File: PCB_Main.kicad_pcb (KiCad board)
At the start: 2 copper layers, 101.6 x 53.3 mm, 37 parts, among them J1 Power, J2 PWM, J3 Analog, J4 PWM, J5 Analog, J6 Communication, J7 Conn_01x03, J8 Conn_01x03, U1 DPS310, U2 ATP3012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

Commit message: update silk
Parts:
- 1PPS1: value LED -> 1PPS
- AE-MICRO-SD-DIP1: value Micro_SD_Card_Det_Hirose_DM3AT -> AE-MICRO-SD-DIP
- Air-UART1: value Conn_01x04_Female -> Air-UART
- Air1: value LED -> Air
- GPS-UART1: value Conn_01x05_Female -> GPS-UART
- ICS-UART1: value Conn_01x05_Female -> ICS-UART
- ICS1: value LED -> ICS
- M78AR05-1: renamed from U3; value R-78E5.0-1.0 -> M78AR05
- M78AR05-2: renamed from U5; value R-78E5.0-1.0 -> M78AR05
- M78AR05-3: renamed from U4; value R-78E5.0-1.0 -> M78AR05
- Power1: value LED -> Power
- SD1: value LED -> SD
- Speaker1: value Conn_01x03_Female -> Speaker
- Under-UART1: value Conn_01x04_Female -> Under-UART
- Under1: value LED -> Under
- renumbered U6 to AE-BNO55, U2 to ATP3012, U1 to DPS310, U7 to ICS-board1
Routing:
- net L_Air: track 43.7 -> 45.1 mm
- net L_ICS: track 21.0 -> 21.9 mm
- added copper zone on B.Cu, net GND
- added copper zone on F.Cu, net GND

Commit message: pass DRC
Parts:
- moved Power1 3.18 mm to (124.8, 97.5), turned to 180 degrees
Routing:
- net 3.3V: track 182.2 -> 184.5 mm
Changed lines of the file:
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@@
     (pad_to_mask_clearance 0)
     (aux_axis_origin 100 100)
-    (grid_origin 100 100)
     (pcbplotparams
       (layerselection 0x0000030_80000001)
@@
   )
   (footprint "LED_THT:LED_D3.0mm_Clear" (layer "F.Cu")
-    (at 121.59 97.46)
+    (at 124.77 97.46 180)
     (descr "IR-LED, diameter 3.0mm, 2 pins, color: clear")
     (tags "IR infrared LED diameter 3.0mm 2 pins clear")
@@
       (effects (font (size 1 1) (thickness 0.15)))
     )
-    (fp_text value "Power" (at -3.175 0) (layer "F.SilkS")
+    (fp_text value "Power" (at 6.355 0) (layer "F.SilkS")
       (effects (font (size 1 1) (thickness 0.15)))
     )
@@
     (fp_arc (start -0.23 -1.16619) (mid 3.17 0.000452) (end -0.230555 1.165476) (layer "F.Fab") (width 0.1))
     (fp_circle (center 1.27 0) (end 2.77 0) (layer "F.Fab") (width 0.1) (fill none))
-    (pad "1" thru_hole rect (at 0 0) (size 1.8 1.8) (drill 0.9) (layers *.Cu *.Mask)
+    (pad "1" thru_hole rect (at 0 0 180) (size 1.8 1.8) (drill 0.9) (layers *.Cu *.Mask)
       (net 1 "GND") (pinfunction "K") (pintype "passive"))
-    (pad "2" thru_hole circle (at 2.54 0) (size 1.8 1.8) (drill 0.9) (layers *.Cu *.Mask)
+    (pad "2" thru_hole circle (at 2.54 0 180) (size 1.8 1.8) (drill 0.9) (layers *.Cu *.Mask)
       (net 47 "3.3V") (pinfunction "A") (pintype "passive"))
     (model "${KICAD6_3DMODEL_DIR}/LED_THT.3dshapes/LED_D3.0mm_Clear.wrl"
@@
   (segment (start 189.18 75.87) (end 189.26 75.79) (width 0.25) (layer "F.Cu") (net 1))
   (segment (start 145.64 87.3) (end 145.72 87.3) (width 0.25) (layer "F.Cu") (net 1))
-  (segment (start 119.68 93.655) (end 119.685 93.65) (width 0.25) (layer "F.Cu") (net 1))
   (segment (start 126.416 49.2) (end 128.321 51.105) (width 0.25) (layer "F.Cu") (net 1))
   (segment (start 178.555 83.04) (end 168.58 83.04) (width 0.25) (layer "F.Cu") (net 1))
@@
   (segment (start 141.275 51.105) (end 141.91 51.105) (width 0.25) (layer "F.Cu") (net 1))
   (segment (start 113.97 74.6) (end 116.51 74.6) (width 0.25) (layer "F.Cu") (net 1))
+  (segment (start 121.59 93.65) (end 107.62 93.65) (width 0.25) (layer "F.Cu") (net 1))
   (segment (start 189.26 59.32) (end 191.4 59.32) (width 0.25) (layer "F.Cu") (net 1))
   (segment (start 107.62 84.76) (end 107.62 92.38) (width 0.25) (layer "F.Cu") (net 1))
   (segment (start 107.62 92.38) (end 107.62 97.46) (width 0.25) (layer "F.Cu") (net 1))
   (segment (start 166.04 80.5) (end 168.58 83.04) (width 0.25) (layer "F.Cu") (net 1))
-  (segment (start 107.62 93.65) (end 119.685 93.65) (width 0.25) (layer "F.Cu") (net 1))
+  (segment (start 121.59 93.65) (end 124.765 93.65) (width 0.25) (layer "F.Cu") (net 1))
   (segment (start 157.15 56.82) (end 157.15 52.375) (width 0.25) (layer "F.Cu") (net 1))
   (segment (start 191.44 75.87) (end 189.34 75.87) (width 0.25) (layer "F.Cu") (net 1))
@@
   (segment (start 110.16 54.28) (end 108.89 54.28) (width 0.25) (layer "F.Cu") (net 1))
   (segment (start 141.91 51.105) (end 141.91 59.34) (width 0.25) (layer "F.Cu") (net 1))
-  (segment (start 119.685 93.65) (end 121.59 93.65) (width 0.25) (layer "F.Cu") (net 1))
   (segment (start 107.62 55.55) (end 107.615 55.545) (width 0.25) (layer "F.Cu") (net 1))
   (segment (start 141.275 51.105) (end 148.915 51.105) (width 0.25) (layer "F.Cu") (net 1))
@@
   (segment (start 153.35 60.62) (end 157.15 56.82) (width 0.25) (layer "F.Cu") (net 1))
   (segment (start 166.04 74.6) (end 166.04 80.5) (width 0.25) (layer "F.Cu") (net 1))
+  (segment (start 124.77 97.46) (end 124.77 93.655) (width 0.25) (layer "F.Cu") (net 1))
   (segment (start 134.45 93.65) (end 135.6 92.5) (width 0.25) (layer "F.Cu") (net 1))
   (segment (start 135.6 77.26) (end 135.6 72.1) (width 0.25) (layer "F.Cu") (net 1))
+  (segment (start 124.765 93.65) (end 134.45 93.65) (width 0.25) (layer "F.Cu") (net 1))
   (segment (start 107.62 92.38) (end 107.62 93.65) (width 0.25) (layer "F.Cu") (net 1))
   (segment (start 113.97 58.09) (end 116.51 58.09) (width 0.25) (layer "F.Cu") (net 1))
@@
   (segment (start 157.15 52.375) (end 155.88 51.105) (width 0.25) (layer "F.Cu") (net 1))
   (segment (start 145.72 94.92) (end 143.18 97.46) (width 0.25) (layer "F.Cu") (net 1))
-  (segment (start 121.59 93.65) (end 134.45 93.65) (width 0.25) (layer "F.Cu") (net 1))
   (segment (start 128.321 51.105) (end 141.275 51.105) (width 0.25) (layer "F.Cu") (net 1))
   (segment (start 189.34 75.87) (end 189.26 75.79) (width 0.25) (layer "F.Cu") (net 1))
@@
   (segment (start 113.97 88.57) (end 110.16 84.76) (width 0.25) (layer "F.Cu") (net 1))
   (segment (start 107.62 84.76) (end 110.16 84.76) (width 0.25) (layer "F.Cu") (net 1))
-  (segment (start 121.59 97.46) (end 121.59 93.65) (width 0.25) (layer "F.Cu") (net 1))
   (segment (start 191.4 59.32) (end 191.44 59.36) (width 0.25) (layer "F.Cu") (net 1))
   (segment (start 110.16 70.79) (end 113.97 74.6) (width 0.25) (layer "F.Cu") (net 1))
@@
   (segment (start 155.88 51.105) (end 148.915 51.105) (width 0.25) (layer "F.Cu") (net 1))
   (segment (start 153.34 68.25) (end 154.61 66.98) (width 0.25) (layer "F.Cu") (net 1))
+  (segment (start 124.77 93.655) (end 124.765 93.65) (width 0.25) (layer "F.Cu") (net 1))
   (segment (start 141.275 62.535) (end 136.195 62.535) (width 0.25) (layer "B.Cu") (net 1))
   (segment (start 189.26 75.79) (end 180.09 75.79) (width 0.25) (layer "B.Cu") (net 1))
@@
   (segment (start 144.45 84.125) (end 119.685 84.125) (width 0.25) (layer "B.Cu") (net 31))
   (segment (start 167.945 49.2) (end 164.77 52.375) (width 0.25) (layer "B.Cu") (net 31))
-  (segment (start 119.05 86.03) (end 116.51 86.03) (width 0.25) (layer "F.Cu") (net 32))
-  (segment (start 136.83 86.03) (end 119.05 86.03) (width 0.25) (layer "F.Cu") (net 32))
-  (segment (start 143.22 92.5) (end 136.83 86.11) (width 0.25) (layer "F.Cu") (net 32))
-  (segment (start 119.05 58.09) (end 119.05 86.03) (width 0.25) (layer "F.Cu") (net 32))
+  (segment (start 119.05 86.03) (end 116.51 86.03) (width 1) (layer "F.Cu") (net 32))
+  (segment (start 136.83 86.03) (end 119.05 86.03) (width 1) (layer "F.Cu") (net 32))
+  (segment (start 143.22 92.5) (end 136.83 86.11) (width 1) (layer "F.Cu") (net 32))
+  (segment (start 119.05 58.09) (end 119.05 86.03) (width 1) (layer "F.Cu") (net 32))
   (segment (start 136.83 86.11) (end 136.83 86.03) (width 0.25) (layer "F.Cu") (net 32))
-  (segment (start 116.51 55.55) (end 119.05 58.09) (width 0.25) (layer "F.Cu") (net 32))
-  (segment (start 116.51 72.06) (end 119.05 72.06) (width 0.25) (layer "F.Cu") (net 32))
+  (segment (start 116.51 55.55) (end 119.05 58.09) (width 1) (layer "F.Cu") (net 32))
+  (segment (start 116.51 72.06) (end 119.05 72.06) (width 1) (layer "F.Cu") (net 32))
   (segment (start 145.64 94.92) (end 145.72 94.92) (width 0.25) (layer "B.Cu") (net 32))
-  (segment (start 143.22 92.5) (end 145.64 94.92) (width 0.25) (layer "B.Cu") (net 32))
-  (segment (start 145.72 94.92) (end 145.72 97.46) (width 0.25) (layer "B.Cu") (net 32))
+  (segment (start 143.22 92.5) (end 145.64 94.92) (width 1) (layer "B.Cu") (net 32))
+  (segment (start 145.72 94.92) (end 145.72 97.46) (width 1) (layer "B.Cu") (net 32))
   (segment (start 110.16 87.3) (end 113.97 91.11) (width 0.25) (layer "F.Cu") (net 35))
   (segment (start 113.97 91.11) (end 116.51 91.11) (width 0.25) (layer "F.Cu") (net 35))
@@
   (segment (start 140.025 54.915) (end 145.73 60.62) (width 0.25) (layer "B.Cu") (net 47))
   (segment (start 178.105 88.57) (end 185.09 81.585) (width 0.25) (layer "B.Cu") (net 47))
-  (segment (start 124.13 97.46) (end 126.035 95.555) (width 0.25) (layer "B.Cu") (net 47))
   (segment (start 135.56 95.555) (end 136.83 94.285) (width 0.25) (layer "B.Cu") (net 47))
   (segment (start 145.73 60.62) (end 141.91 64.44) (width 0.25) (layer "B.Cu") (net 47))
@@
   (segment (start 140.68 92.5) (end 140.68 91.15) (width 0.25) (layer "B.Cu") (net 47))
   (segment (start 140.68 91.15) (end 140.64 91.11) (width 0.25) (layer "B.Cu") (net 47))
+  (segment (start 135.56 95.555) (end 123.495 95.555) (width 0.25) (layer "B.Cu") (net 47))
   (segment (start 160.97 58.08) (end 160.97 60.62) (width 0.25) (layer "B.Cu") (net 47))
   (segment (start 141.91 64.44) (end 138.1 64.44) (width 0.25) (layer "B.Cu") (net 47))
   (segment (start 136.83 94.285) (end 138.895 94.285) (width 0.25) (layer "B.Cu") (net 47))
+  (segment (start 123.495 95.555) (end 122.23 96.82) (width 0.25) (layer "B.Cu") (net 47))
   (segment (start 130.48 53.01) (end 126.67 53.01) (width 0.25) (layer "B.Cu") (net 47))
-  (segment (start 126.035 95.555) (end 135.56 95.555) (width 0.25) (layer "B.Cu") (net 47))
   (segment (start 132.385 54.915) (end 140.025 54.915) (width 0.25) (layer "B.Cu") (net 47))
   (segment (start 130.48 53.01) (end 132.385 54.915) (width 0.25) (layer "B.Cu") (net 47))
+  (segment (start 122.23 96.82) (end 122.23 97.46) (width 0.25) (layer "B.Cu") (net 47))
   (segment (start 193.98 81.764569) (end 193.98 56.82) (width 0.25) (layer "F.Cu") (net 51))
   (segment (start 133.02 64.44) (end 134.925 62.535) (width 0.25) (layer "F.Cu") (net 51))
@@
     (polygon
       (pts
-        (xy 207.95 101.905)
-        (xy 95.555 102.54)
-        (xy 96.19 42.85)
-        (xy 207.95 42.85)
+        (xy 206.045 103.175)
+        (xy 93.65 103.81)
+        (xy 94.285 44.12)
+        (xy 206.045 44.12)
       )
     )

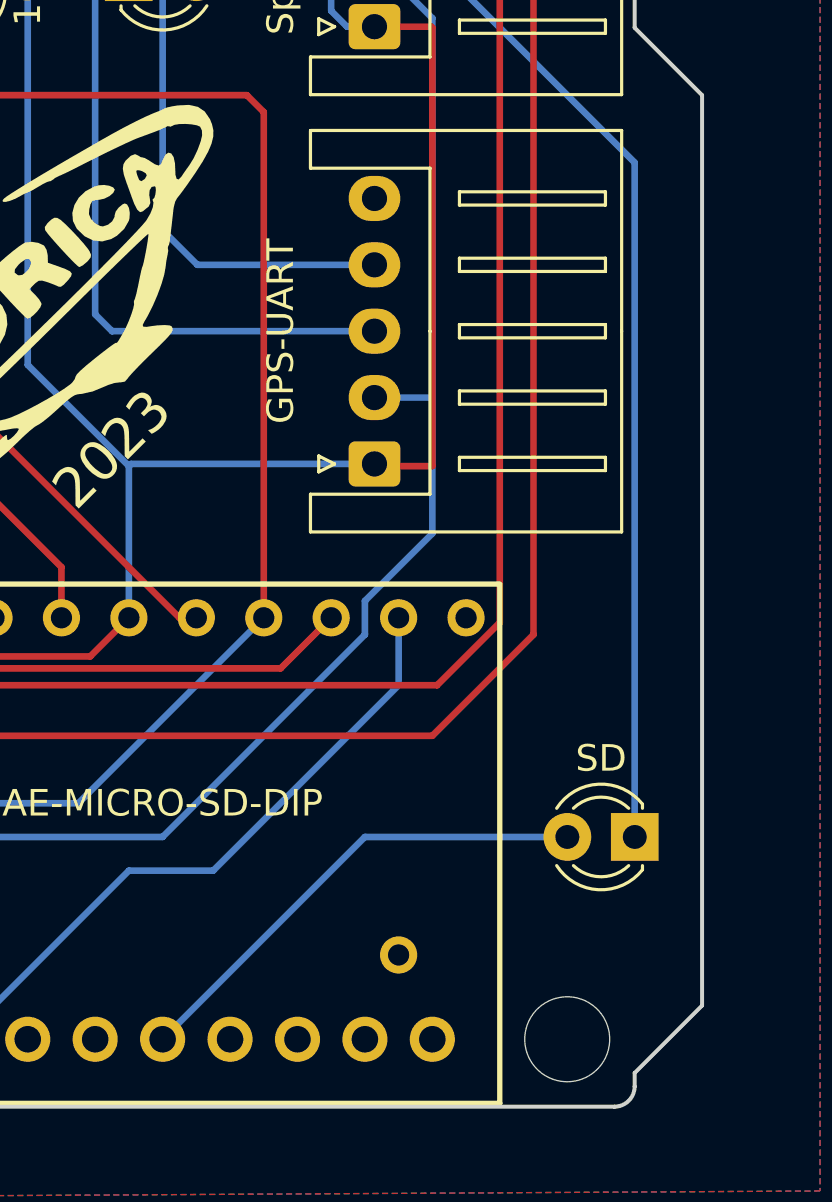
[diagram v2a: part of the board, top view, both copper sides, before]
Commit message: add capacitor
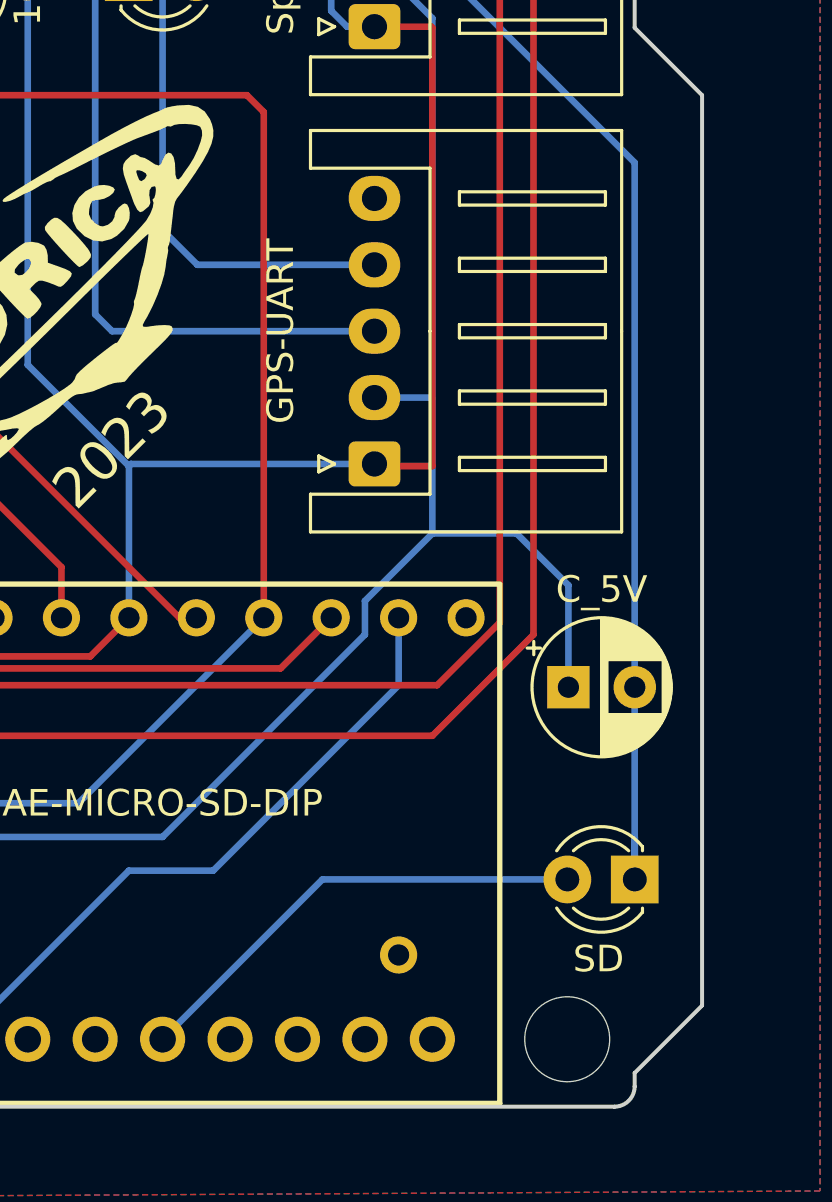
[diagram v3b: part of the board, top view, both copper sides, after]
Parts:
- added C1: C_5V, Capacitor_THT:CP_Radial_D5.0mm_P2.50mm, F.Cu at (196.6, 84.2)
- moved LED1 1.60 mm to (199.1, 91.4)
- renumbered SD1 to LED1, ICS1 to LED2, Air1 to LED3, Under1 to LED4, Power1 to LED5, 1PPS1 to LED6
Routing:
- net 5V: track 88.9 -> 98.7 mm
- net GND: track 451.1 -> 454.3 mm
- net L_SD: track 18.4 -> 17.7 mm
